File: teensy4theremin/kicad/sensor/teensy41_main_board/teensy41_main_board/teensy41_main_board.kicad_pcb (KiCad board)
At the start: 2 copper layers, 139.7 x 61 mm, 9 parts, among them J1 Conn_02x20_Odd_Even, J2 AudioJack3, J3 AudioJack3, J4 Conn_01x03_Male, J5 Conn_01x03_Male, J6 Conn_01x02_Male, U1 Teensy41, U2 TeensyAudioD, U3 PLT133T10W

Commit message: main board pcb
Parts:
- added J7: AudioJack3, Connector_Audio:Jack_3.5mm_CUI_SJ1-3533NG_Horizontal, F.Cu at (133.9, 69.8)
- added J8: AudioJack3, Connector_Audio:Jack_6.35mm_ST_008G_04, F.Cu at (160.0, 74.9)
- moved J5 16.6 mm to (174.0, 97.8)
- moved J4 2.54 mm to (41.9, 83.8)
- moved J6 1.80 mm to (52.1, 71.1), turned to 270 degrees
- moved J3 1.31 mm to (132.1, 74.9)
- moved U3 1.27 mm to (146.1, 78.7)
- moved J2 0.73 mm to (119.4, 69.8)
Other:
- outline, holes or cut-outs redrawn

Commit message: main boark kicad
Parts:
- added C1: 1uF, Capacitor_SMD:C_0805_2012Metric_Pad1.18x1.45mm_HandSolder, B.Cu at (44.5, 106.7)
- added C2: 1uF, Capacitor_SMD:C_0805_2012Metric_Pad1.18x1.45mm_HandSolder, B.Cu at (156.8, 109.9)
- added C3: 10nF, Capacitor_SMD:C_0805_2012Metric_Pad1.18x1.45mm_HandSolder, B.Cu at (44.5, 110.5)
- added C4: 10nF, Capacitor_SMD:C_0805_2012Metric_Pad1.18x1.45mm_HandSolder, B.Cu at (160.9, 110.5)
- added C5: 1uF, Capacitor_SMD:C_0805_2012Metric_Pad1.18x1.45mm_HandSolder, B.Cu at (40.6, 118.1)
- added C6: 1uF, Capacitor_SMD:C_0805_2012Metric_Pad1.18x1.45mm_HandSolder, B.Cu at (161.9, 114.3)
- added C7: 0.1uF, Capacitor_SMD:C_0805_2012Metric_Pad1.18x1.45mm_HandSolder, B.Cu at (156.6, 81.9)
- added C8: 0.1uF, Capacitor_SMD:C_0805_2012Metric_Pad1.18x1.45mm_HandSolder, B.Cu at (142.9, 85.1)
- added C9: 0.1uF, Capacitor_SMD:C_0805_2012Metric_Pad1.18x1.45mm_HandSolder, B.Cu at (148.0, 85.1)
- added J10: AUDIO_OUT_EXT, Connector_PinHeader_2.54mm:PinHeader_1x12_P2.54mm_Vertical, F.Cu at (81.3, 109.2)
- added J12: SPDIF_IN2, Connector_PinHeader_2.54mm:PinHeader_1x08_P2.54mm_Vertical, F.Cu at (116.8, 86.4)
- added J9: SPDIF_IN, Connector_PinHeader_2.54mm:PinHeader_1x08_P2.54mm_Vertical, F.Cu at (161.3, 86.4)
- added R1: 200, Resistor_SMD:R_0805_2012Metric_Pad1.20x1.40mm_HandSolder, B.Cu at (145.4, 89.9)
- added SW1: SW_Push, Button_Switch_THT:SW_Tactile_SKHH_Angled, F.Cu at (64.1, 71.1)
- added U4: LD3985M47R_SOT23, Package_TO_SOT_SMD:SOT-23-5, B.Cu at (40.8, 114.1)
- added U5: LD3985M47R_SOT23, Package_TO_SOT_SMD:SOT-23-5, B.Cu at (158.1, 114.3)
- J1: value Conn_02x20_Odd_Even -> LCD_CONTROLS
- J2: value AudioJack3 -> LINE_IN
- J3: value AudioJack3 -> LINE_OUT_BIG
- J4: value Conn_01x03_Male -> VOL_SENSOR
- J5: value Conn_01x03_Male -> PITCH_SENSOR
- J6: value Conn_01x02_Male -> POWER_IN
- J7: value AudioJack3 -> LINE_OUT_35
- J8: value AudioJack3 -> EXPR_PED
- moved J4 34.4 mm to (44.5, 118.1)
- moved J5 17.6 mm to (165.1, 113.0)
- moved J8 15.3 mm to (145.4, 79.4)
- moved U3 12.1 mm to (158.1, 78.7)
- moved J3 4.63 mm to (130.8, 79.4)
- moved J6 2.62 mm to (52.7, 73.7)
- moved J1 2.29 mm to (50.2, 85.1)
- moved J7 2.21 mm to (132.1, 68.6)
- moved J2 1.80 mm to (118.1, 68.6)
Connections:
- net Net-(J2-PadR) renamed /LIN_R
- net Net-(J2-PadT) renamed /LIN_L
- net Net-(J3-PadR) renamed /LOUT_R
- net Net-(J3-PadT) renamed /LOUT_L
- J1 pad 1: Net-(J1-Pad1) -> /VIN
- J1 pad 10: Net-(J1-Pad10) -> /TOUCH_IRQ
- J1 pad 11: Net-(J1-Pad11) -> /LCD_CS
- J1 pad 12: Net-(J1-Pad12) -> /LCD_MOSI
- J1 pad 13: Net-(J1-Pad13) -> /LCD_SCK
- J1 pad 14: Net-(J1-Pad14) -> /LCD_MISO
- J1 pad 15: Net-(J1-Pad15) -> /3V3
- J1 pad 16: Net-(J1-Pad16) -> /POT1
- J1 pad 17: Net-(J1-Pad17) -> /ENC1_C
- J1 pad 18: Net-(J1-Pad18) -> /POT2
- J1 pad 19: Net-(J1-Pad19) -> /ENC2_C
- J1 pad 2: Net-(J1-Pad2) -> GND
- J1 pad 20: Net-(J1-Pad20) -> /POT3
- J1 pad 21: Net-(J1-Pad21) -> /ENC3_C
- J1 pad 22: Net-(J1-Pad22) -> /POT4
- J1 pad 23: Net-(J1-Pad23) -> /ENC4_C
- J1 pad 24: Net-(J1-Pad24) -> /POT5
- J1 pad 25: Net-(J1-Pad25) -> /ENC4_A
- J1 pad 26: Net-(J1-Pad26) -> /TOUCH_CS
- J1 pad 27: Net-(J1-Pad27) -> /ENC4_B
- J1 pad 28: Net-(J1-Pad28) -> /BTN_1
- J1 pad 29: Net-(J1-Pad29) -> /BTN_3
- J1 pad 3: Net-(J1-Pad3) -> /ENC1_A
- J1 pad 30: Net-(J1-Pad30) -> /BTN_2
- J1 pad 4: Net-(J1-Pad4) -> /ENC1_B
- J1 pad 5: Net-(J1-Pad5) -> /ENC2_A
- J1 pad 6: Net-(J1-Pad6) -> /ENC2_B
- J1 pad 7: Net-(J1-Pad7) -> /ENC3_A
- J1 pad 8: Net-(J1-Pad8) -> /ENC3_B
- J1 pad 9: Net-(J1-Pad9) -> /LCD_DC
- J2 pad S: Net-(J2-PadS) -> GND
- J3 pad S: Net-(J3-PadS) -> GND
- J4 pad 1: Net-(J4-Pad1) -> /VCC_VOL
- J4 pad 2: Net-(J4-Pad2) -> /VOL_OSC
- J4 pad 3: Net-(J4-Pad3) -> GND
- J5 pad 1: Net-(J5-Pad1) -> /VCC_PITCH
- J5 pad 2: Net-(J5-Pad2) -> /PITCH_OSC
- J5 pad 3: Net-(J5-Pad3) -> GND
- J6 pad 1: Net-(J6-Pad1) -> GND
- J6 pad 2: Net-(J6-Pad2) -> /VIN
- J7 pad S: Net-(J3-PadS) -> GND
- J8 pad S: Net-(J8-PadS) -> GND
- J8 pad T: Net-(J8-PadT) -> /EXPR_PED
- U1 pad 1: Net-(U1-Pad1) -> GND
- U1 pad 10: Net-(U1-Pad10) -> /I2S_DIN1
- U1 pad 11: Net-(U1-Pad11) -> /I2S_DOUT1C
- U1 pad 12: Net-(U1-Pad12) -> /LCD_CS
- U1 pad 13: Net-(U1-Pad13) -> /LCD_MOSI
- U1 pad 14: Net-(U1-Pad14) -> /LCD_MISO
- U1 pad 15: Net-(U1-Pad15) -> /3V3
- U1 pad 16: Net-(U1-Pad16) -> /TOUCH_IRQ
- U1 pad 17: Net-(U1-Pad17) -> /LCD_DC
- U1 pad 18: Net-(U1-Pad18) -> /ENC1_C
- U1 pad 19: Net-(U1-Pad19) -> /ENC2_C
- U1 pad 2: Net-(U1-Pad2) -> /ENC1_A
- U1 pad 20: Net-(U1-Pad20) -> /ENC3_C
- U1 pad 21: Net-(U1-Pad21) -> /ENC4_C
- U1 pad 22: Net-(U1-Pad22) -> /ENC4_A
- U1 pad 23: Net-(U1-Pad23) -> /ENC4_B
- U1 pad 24: Net-(U1-Pad24) -> /BTN_3
- U1 pad 25: Net-(U1-Pad25) -> /VOL_OSC
- U1 pad 26: Net-(U1-Pad26) -> /BTN_2
- U1 pad 27: Net-(U1-Pad27) -> /BTN_1
- U1 pad 28: Net-(U1-Pad28) -> /PITCH_OSC
- U1 pad 29: Net-(U1-Pad29) -> /TOUCH_CS
- U1 pad 3: Net-(U1-Pad3) -> /ENC1_B
- U1 pad 30: Net-(U1-Pad30) -> /POT5
- U1 pad 31: Net-(U1-Pad31) -> /POT4
- U1 pad 32: Net-(U1-Pad32) -> /POT3
- U1 pad 33: Net-(U1-Pad33) -> /POT2
- U1 pad 34: Net-(U1-Pad34) -> GND
- U1 pad 35: Net-(U1-Pad35) -> /LCD_SCK
- U1 pad 36: Net-(U1-Pad36) -> /SPDIF_OUT
- U1 pad 37: Net-(U1-Pad37) -> /SPDIF_IN
- U1 pad 38: Net-(U1-Pad38) -> /POT1
- U1 pad 39: Net-(U1-Pad39) -> /EXPR_PED
- U1 pad 4: Net-(U1-Pad4) -> /ENC2_A
- U1 pad 40: Net-(U1-Pad40) -> /I2C_SDA
- U1 pad 41: Net-(U1-Pad41) -> /I2C_SCL
- U1 pad 42: Net-(U1-Pad42) -> /I2S_LRCK
- U1 pad 43: Net-(U1-Pad43) -> /I2S_BCLK
- U1 pad 44: Net-(U1-Pad44) -> /PIN22
- U1 pad 45: Net-(U1-Pad45) -> /I2S_MCLK
- U1 pad 46: Net-(U1-Pad46) -> /3V3
- U1 pad 47: Net-(U1-Pad47) -> GND
- U1 pad 48: Net-(U1-Pad48) -> /VIN
- U1 pad 5: Net-(U1-Pad5) -> /ENC2_B
- U1 pad 6: Net-(U1-Pad6) -> /ENC3_A
- U1 pad 7: Net-(U1-Pad7) -> /ENC3_B
- U1 pad 8: Net-(U1-Pad8) -> /I2S_DOUT1D
- U1 pad 9: Net-(U1-Pad9) -> /I2S_DOUT1A
- U2 pad 1: Net-(U2-Pad1) -> GND
- U2 pad 10: Net-(U2-Pad10) -> /I2S_DIN1
- U2 pad 20: Net-(U2-Pad20) -> /I2C_SDA
- U2 pad 21: Net-(U2-Pad21) -> /I2C_SCL
- U2 pad 22: Net-(U2-Pad22) -> /I2S_LRCK
- U2 pad 23: Net-(U2-Pad23) -> /I2S_BCLK
- U2 pad 25: Net-(U2-Pad25) -> /I2S_MCLK
- U2 pad 26: Net-(U2-Pad26) -> /3V3
- U2 pad 27: Net-(U2-Pad27) -> GND
- U2 pad 32: Net-(J3-PadS) -> GND
- U2 pad 37: Net-(J2-PadS) -> GND
- U2 pad 38: Net-(J2-PadS) -> GND
- U2 pad 9: Net-(U2-Pad9) -> /I2S_DOUT1A
- U3 pad 1: Net-(U3-Pad1) -> /SPDIF_OUT
- U3 pad 2: Net-(U3-Pad2) -> /3V3
- U3 pad 3: Net-(U3-Pad3) -> GND
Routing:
- net GND: track 0.00 -> 329.3 mm, vias 0 -> 1
- net /VIN: track 0.00 -> 134.7 mm
- net /PIN22: track 0.00 -> 121.5 mm, vias 0 -> 3
- net /SPDIF_OUT: track 0.00 -> 117.5 mm
- net /3V3: track 0.00 -> 105.3 mm
- net /EXPR_PED: track 0.00 -> 102.4 mm
- net /SPDIF_IN: track 0.00 -> 99.9 mm, vias 0 -> 1
- net /PITCH_OSC: track 0.00 -> 93.0 mm
- net /LOUT_L: track 0.00 -> 66.2 mm
- net /I2S_MCLK: track 0.00 -> 64.8 mm, vias 0 -> 1
- net /LOUT_R: track 0.00 -> 60.8 mm
- net /I2S_BCLK: track 0.00 -> 60.0 mm, vias 0 -> 1
- net /I2S_LRCK: track 0.00 -> 57.7 mm, vias 0 -> 1
- net /I2S_DOUT1D: track 0.00 -> 56.6 mm, vias 0 -> 2
- net /I2C_SCL: track 0.00 -> 55.4 mm, vias 0 -> 1
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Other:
- board size 139.7 x 61 mm -> 133.3 x 61 mm

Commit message: main board
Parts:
- added J11: Grounding, Connector_PinHeader_2.54mm:PinHeader_1x01_P2.54mm_Vertical, F.Cu at (43.8, 77.5)
- added J13: ProtoGrid, Module:Teensy41ThereminProtoGrid, F.Cu at (81.3, 111.8)
- moved R1 3.83 mm to (141.6, 89.5), turned to 0 degrees
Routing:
- net GND: track 329.3 -> 592.4 mm, vias 1 -> 4
- net /3V3: track 105.3 -> 187.7 mm, vias 0 -> 1
- net /VIN: track 134.7 -> 215.0 mm, vias 0 -> 1
- net /PITCH_OSC: track 93.0 -> 98.1 mm
- net /VCC_PITCH: track 3.08 -> 7.21 mm
- net Net-(C8-Pad1): track 4.63 -> 8.49 mm
- net /SPDIF_OUT: track 117.5 -> 120.9 mm
- net /SPDIF_IN: track 99.9 -> 101.5 mm
- net /I2S_DOUT1D: track 56.6 -> 55.8 mm
- net /PIN22: track 121.5 -> 122.0 mm
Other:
- outline, holes or cut-outs redrawn
- board text added: "+3.3V"
- board text added: "+5V"
- board text added: "3V3"
- board text added: "4.7V"
- board text added: "BCLK"
- board text added: "BTN1"
- board text added: "BTN2"
- board text added: "DOUT1C"
- board text added: "DOUT1D"
- board text added: "E1A"
- board text added: "E1B"
- board text added: "E1C"
- board text added: "E2A"
- board text added: "E2B"
- board text added: "E3A"
- board text added: "E3B"
- board text added: "EXPR"
- board text added: "EXPR PED"
- board text added: "EXPRESSION PEDAL"
- board text added: "GND"
- board text added: "LCS"
- board text added: "LD/C"
- board text added: "LINE IN"
- board text added: "LINE OUT"
- board text added: "LRCK"
- board text added: "MCLK"
- board text added: "MISO"
- board text added: "MOSI"
- board text added: "OSC"
- board text added: "OUT"
- board text added: "PIN 22"
- board text added: "PIN22"
- board text added: "PITCH"
- board text added: "POT1"
- board text added: "POT2"
- board text added: "POT3"
- board text added: "POT4"
- board text added: "POT5"
- board text added: "PRG"
- board text added: "S/PDIF"
- board text added: "S/PDIF OUT"
- board text added: "SCK"
- board text added: "SCL"
- board text added: "SDA"
- board text added: "SPDIF IN"
- board text added: "SPDIFIN"
- board text added: "SPDIFOUT"
- board text added: "SPDOUT"
- board text added: "TCS"
- board text added: "TIRQ"
- board text added: "Teensy 4.1"
- board text added: "Teensy 4.1 Theremin Main Board rev 0.1 (c) Vadim Lopatin 2020"
- board text added: "Teensy Audio Adaptor D"
- board text added: "VOL"
- board text added: "VOLUME"

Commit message: update pcb
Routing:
- net /EXPR_PED: track 102.4 -> 104.2 mm
- added copper zone on B.Cu, net GND
- added copper zone on F.Cu, net GND
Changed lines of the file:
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@@
     (thickness 1.6)
     (drawings 139)
-    (tracks 499)
+    (tracks 500)
     (zones 0)
     (modules 29)
@@
   (layers
     (0 F.Cu signal)
-    (31 B.Cu signal)
+    (31 B.Cu signal hide)
     (32 B.Adhes user)
     (33 F.Adhes user)
@@
     (last_trace_width 0.25)
     (trace_clearance 0.2)
-    (zone_clearance 0.508)
+    (zone_clearance 0.3)
     (zone_45_only no)
     (trace_min 0.2)
@@
   (segment (start 142.605 94.065) (end 142.915 94.375) (width 0.25) (layer B.Cu) (net 47))
   (segment (start 142.605 89.535) (end 142.605 94.065) (width 0.25) (layer B.Cu) (net 47))
-  (segment (start 147.915 94.375) (end 147.915 97.115) (width 0.25) (layer B.Cu) (net 48))
-  (segment (start 147.955 97.155) (end 147.915 97.115) (width 0.25) (layer B.Cu) (net 48))
-  (segment (start 154.305 97.155) (end 154.94 96.52) (width 0.25) (layer B.Cu) (net 48))
-  (segment (start 123.825 97.155) (end 154.305 97.155) (width 0.25) (layer B.Cu) (net 48))
-  (segment (start 123.19 96.52) (end 123.825 97.155) (width 0.25) (layer B.Cu) (net 48))
-  (segment (start 154.94 96.52) (end 161.29 96.52) (width 0.25) (layer B.Cu) (net 48))
-  (segment (start 116.84 96.52) (end 123.19 96.52) (width 0.25) (layer B.Cu) (net 48))
   (segment (start 110.49 96.52) (end 116.84 96.52) (width 0.25) (layer B.Cu) (net 48))
   (segment (start 106.68 92.71) (end 110.49 96.52) (width 0.25) (layer B.Cu) (net 48))
@@
   (segment (start 147.955 94.335) (end 147.915 94.375) (width 0.25) (layer B.Cu) (net 48))
   (segment (start 147.955 86.1275) (end 147.955 94.335) (width 0.25) (layer B.Cu) (net 48))
+  (segment (start 154.94 96.52) (end 161.29 96.52) (width 0.25) (layer B.Cu) (net 48))
+  (segment (start 153.67 97.79) (end 154.94 96.52) (width 0.25) (layer B.Cu) (net 48))
+  (segment (start 124.46 97.79) (end 153.67 97.79) (width 0.25) (layer B.Cu) (net 48))
+  (segment (start 123.19 96.52) (end 124.46 97.79) (width 0.25) (layer B.Cu) (net 48))
+  (segment (start 116.84 96.52) (end 123.19 96.52) (width 0.25) (layer B.Cu) (net 48))
+  (segment (start 147.955 97.79) (end 147.955 97.155) (width 0.25) (layer B.Cu) (net 48))
+  (segment (start 147.915 97.75) (end 147.955 97.79) (width 0.25) (layer B.Cu) (net 48))
+  (segment (start 147.915 94.375) (end 147.915 97.75) (width 0.25) (layer B.Cu) (net 48))
   (segment (start 52.705 120.65) (end 64.77 120.65) (width 0.25) (layer B.Cu) (net 49))
   (segment (start 64.77 120.65) (end 68.58 124.46) (width 0.25) (layer B.Cu) (net 49))
@@
   (segment (start 66.675 73.66) (end 66.675 78.74) (width 0.25) (layer F.Cu) (net 67))
   (segment (start 64.135 71.12) (end 66.675 73.66) (width 0.25) (layer F.Cu) (net 67))
+  (zone (net 9) (net_name GND) (layer B.Cu) (hatch edge 0.508)
+    (connect_pads (clearance 0.3))
+    (min_thickness 0.2)
+    (fill yes (arc_segments 32) (thermal_gap 0.508) (thermal_bridge_width 0.508))
+    (polygon
+      (pts
+        (xy 171.45 77.47) (xy 165.1 83.82) (xy 165.1 102.87) (xy 171.45 109.22) (xy 171.45 128.27)
+        (xy 38.1 128.27) (xy 38.1 109.22) (xy 44.45 102.87) (xy 44.45 83.82) (xy 38.1 77.47)
+        (xy 38.1 67.31) (xy 171.45 67.31)
+      )
+    )
+  )
+  (zone (net 9) (net_name GND) (layer F.Cu) (hatch edge 0.508)
+    (connect_pads (clearance 0.3))
+    (min_thickness 0.2)
+    (fill yes (arc_segments 32) (thermal_gap 0.508) (thermal_bridge_width 0.508))
+    (polygon
+      (pts
+        (xy 171.45 77.47) (xy 165.1 83.82) (xy 165.1 102.87) (xy 171.45 109.22) (xy 171.45 128.27)
+        (xy 38.1 128.27) (xy 38.1 109.22) (xy 44.45 102.87) (xy 44.45 83.82) (xy 38.1 77.47)
+        (xy 38.1 67.31) (xy 171.45 67.31)
+      )
+    )
+  )
 )

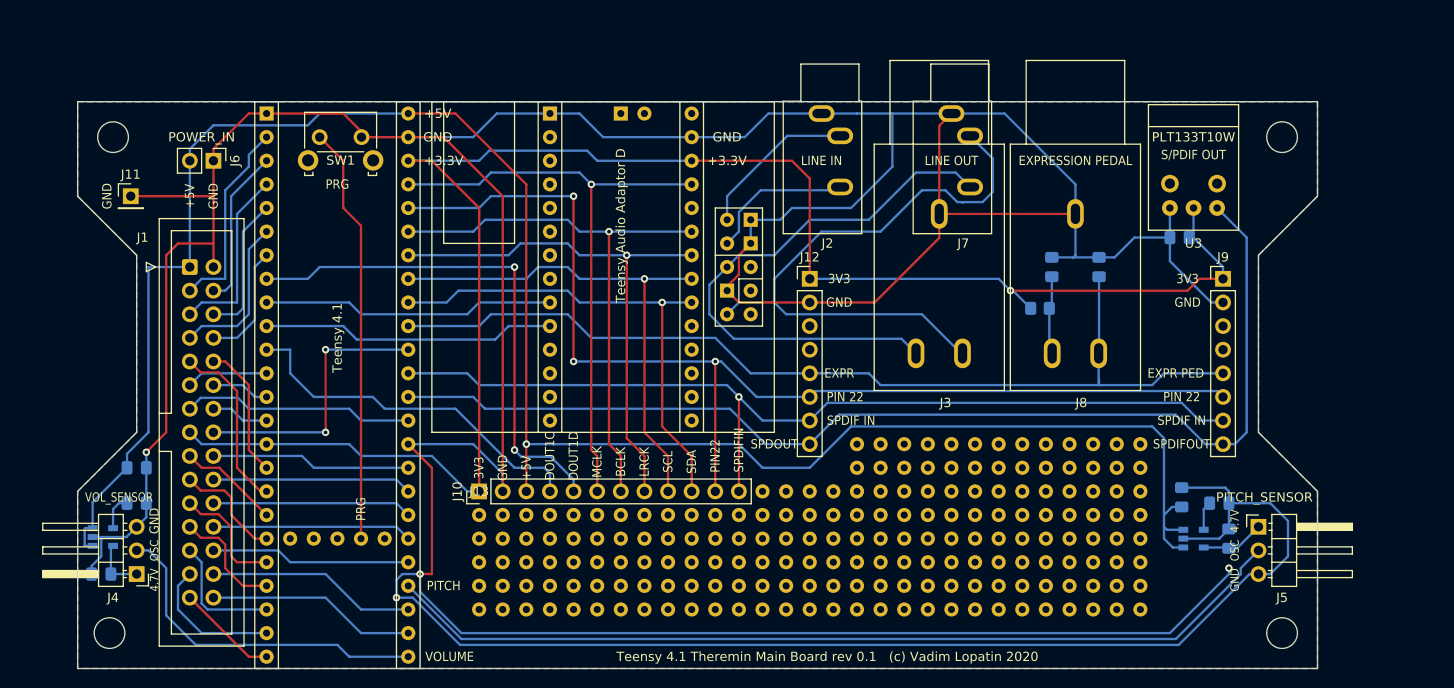
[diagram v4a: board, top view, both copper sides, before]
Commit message: teensy 41 theremin main board and display board rev 0.1
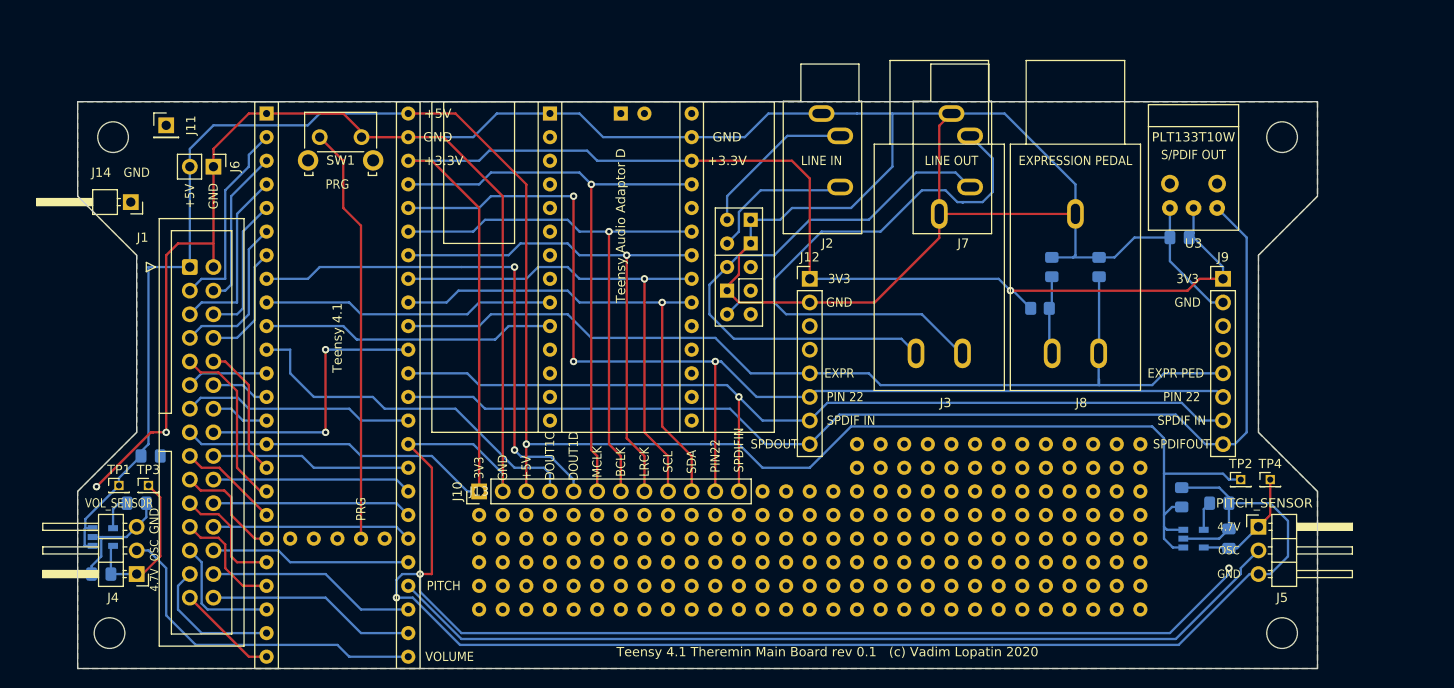
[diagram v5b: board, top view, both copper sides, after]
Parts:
- added J14: Grounding2, Connector_PinHeader_2.54mm:PinHeader_1x01_P2.54mm_Horizontal, F.Cu at (43.8, 78.1)
- added TP1: VIN1, Connector_PinHeader_1.27mm:PinHeader_1x01_P1.27mm_Vertical, F.Cu at (42.5, 108.6)
- added TP2: VIN2, Connector_PinHeader_1.27mm:PinHeader_1x01_P1.27mm_Vertical, F.Cu at (163.2, 108.0)
- added TP3: VCCVOL, Connector_PinHeader_1.27mm:PinHeader_1x01_P1.27mm_Vertical, F.Cu at (45.7, 108.6)
- added TP4: VCCPITCH, Connector_PinHeader_1.27mm:PinHeader_1x01_P1.27mm_Vertical, F.Cu at (166.4, 108.0)
- moved J11 8.52 mm to (47.6, 69.8)
- moved C1 1.97 mm to (46.0, 105.4)
- moved J6 0.64 mm to (52.7, 74.3)
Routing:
- net /VCC_VOL: track 5.90 -> 17.4 mm
- net /VIN: track 215.0 -> 223.8 mm
- net GND: track 592.4 -> 584.5 mm, vias 4 -> 5
- net /VCC_PITCH: track 7.21 -> 12.8 mm
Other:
- board text added: "BTN3"
- board text added: "E2C"
- board text added: "E3C"
- board text added: "E4A"
- board text added: "E4B"
- board text added: "PITCH OSC"
- board text added: "VOL OSC"
- board text removed: "VOL"
